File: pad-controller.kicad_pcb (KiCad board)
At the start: 2 copper layers, 32 parts, among them M1 Motor_Servo, M2 Motor_Servo, M3 Motor_Servo, M4 Motor_Servo, Q1 IRFP450PBF, SW1 SW_Push_Dual, U1 Xbee, U2 TPS56121, U3 LD1117S33TR_SOT223

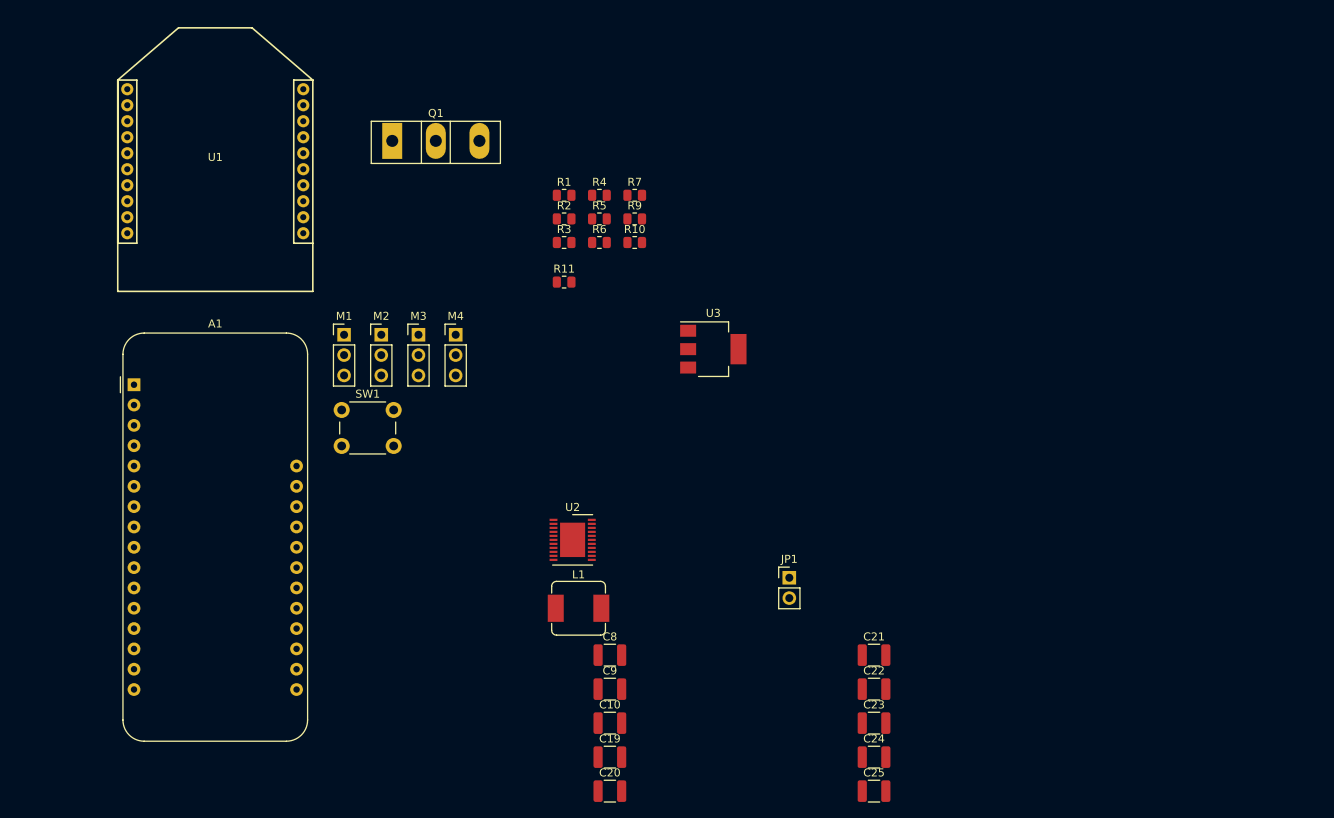
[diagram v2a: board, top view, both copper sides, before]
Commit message: Lay out the buck converter circuitry
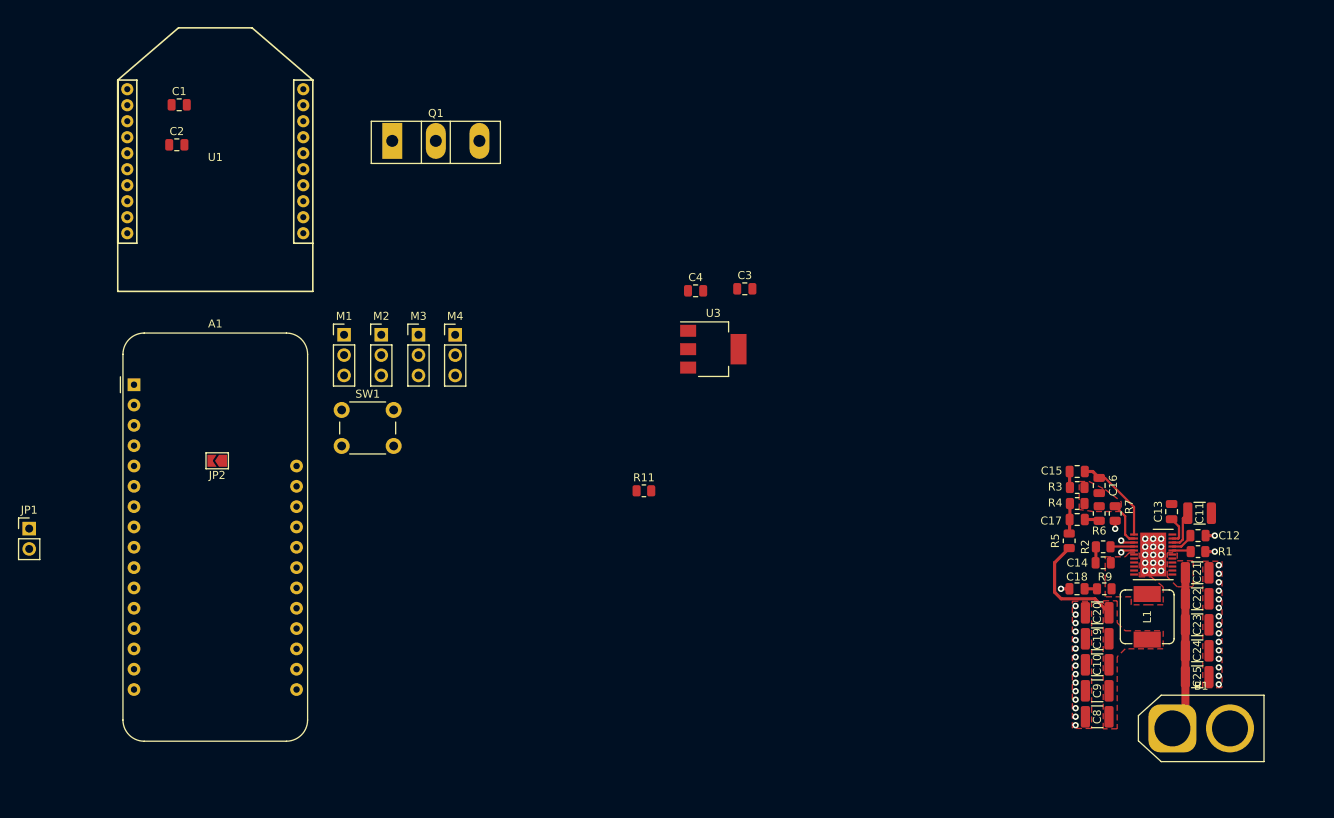
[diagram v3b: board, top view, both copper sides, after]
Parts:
- removed R10: 100 kΩ, Resistor_SMD:R_0805_2012Metric
- added B1: ~, Connector_AMASS:AMASS_XT60-M_1x02_P7.20mm_Vertical, F.Cu at (167.9, 121.7)
- added C1: 47 pF, Capacitor_SMD:C_0805_2012Metric, F.Cu at (43.8, 43.8)
- added C11: 1.0 uF, Capacitor_SMD:C_1210_3225Metric, F.Cu at (171.3, 94.8)
- added C12: 4.7 uF, Capacitor_SMD:C_0805_2012Metric, F.Cu at (171.1, 97.6)
- added C13: 33 nF, Capacitor_SMD:C_0805_2012Metric, F.Cu at (167.8, 94.6)
- added C14: 100 nF, Capacitor_SMD:C_0805_2012Metric, F.Cu at (159.2, 101.0)
- added C15: 390 pF, Capacitor_SMD:C_0805_2012Metric, F.Cu at (156.0, 89.6)
- added C16: 12 pF, Capacitor_SMD:C_0805_2012Metric, F.Cu at (158.8, 91.3)
- added C17: 820 pF, Capacitor_SMD:C_0805_2012Metric, F.Cu at (156.0, 95.6)
- added C18: 1000 pF, Capacitor_SMD:C_0805_2012Metric, F.Cu at (156.0, 104.2)
- added C2: 1 uF, Capacitor_SMD:C_0805_2012Metric, F.Cu at (43.5, 48.8)
- added C3: 10 uF, Capacitor_SMD:C_0805_2012Metric, F.Cu at (114.5, 66.8)
- added C4: 100 nF, Capacitor_SMD:C_0805_2012Metric, F.Cu at (108.3, 67.0)
- added JP2: ~, Jumper:SolderJumper-2_P1.3mm_Open_TrianglePad1.0x1.5mm, F.Cu at (48.5, 88.2)
- moved JP1 95.2 mm to (25.0, 96.7)
- moved R1 90.9 mm to (171.1, 99.6), turned to 180 degrees
- moved R2 78.9 mm to (159.2, 99.0), turned to 180 degrees
- moved R9 74.7 mm to (159.4, 104.2), turned to 180 degrees
- moved U2 72.6 mm to (165.5, 100.0)
- moved R7 72.0 mm to (160.8, 94.8), turned to -90 degrees
- moved R5 71.2 mm to (155.0, 98.2), turned to -90 degrees
- moved L1 71.1 mm to (164.8, 107.8), turned to -90 degrees
- moved R4 71.1 mm to (156.0, 93.6), turned to 180 degrees
- moved R3 71.1 mm to (156.0, 91.6)
- moved R6 71.1 mm to (158.8, 94.8), turned to -90 degrees
- moved C20 64.9 mm to (158.5, 107.2), turned to 180 degrees
- moved C19 62.7 mm to (158.5, 110.5), turned to 180 degrees
- moved C8 61.4 mm to (158.5, 120.2), turned to 180 degrees
- moved C10 61.3 mm to (158.5, 113.8), turned to 180 degrees
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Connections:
- net Net-(U2-ILIM) renamed /Power/ILIM
- A1 pad 17: unconnected-(A1-SDA-Pad17) -> Servo 3 PWM
- A1 pad 18: unconnected-(A1-SCL-Pad18) -> Servo 4 PWM
- A1 pad 19: TIM4 CH4 -> E-Match
- A1 pad 20: TIM4 CH3 -> Launch Inhibit
- A1 pad 21: TIM3 CH2 -> Servo 1 PWM
- A1 pad 22: TIM3 CH1 -> Servo 2 PWM
- A1 pad 9: E-Match -> unconnected-(A1-A4-Pad9)
- M1 pad 2: +3.3V -> +6V
- M1 pad 3: TIM3 CH1 -> Servo 1 PWM
- M2 pad 2: +3.3V -> +6V
- M2 pad 3: TIM3 CH2 -> Servo 2 PWM
- M3 pad 2: +3.3V -> +6V
- M3 pad 3: TIM4 CH3 -> Servo 3 PWM
- M4 pad 2: +3.3V -> +6V
- M4 pad 3: TIM4 CH4 -> Servo 4 PWM
- U2 pad 19: Power Good -> /Power/BP
- U2 pad 21: Net-(U2-EN/SS) -> /Power/EN/SS
- U2 pad 22: Net-(U2-PGOOD) -> unconnected-(U2-PGOOD-Pad22)
- U3 pad 1: unconnected-(U3-GND-Pad1) -> GND
- U3 pad 3: unconnected-(U3-VI-Pad3) -> +6V
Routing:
- net +BATT: track 0.00 -> 25.1 mm
- net +6V: track 0.00 -> 14.1 mm
- net /Power/Compensation: track 0.00 -> 11.4 mm
- net GND: track 0.00 -> 7.80 mm, vias 0 -> 51
- net /Power/Feedback: track 0.00 -> 5.37 mm
- net Net-(C17-Pad1): track 0.00 -> 3.79 mm
- net /Power/EN/SS: track 0.00 -> 3.58 mm
- net Net-(U2-BOOT): track 0.00 -> 2.96 mm
- net /Power/BP: track 0.00 -> 2.95 mm
- net /Power/ILIM: track 0.00 -> 2.35 mm
- net Net-(C14-Pad1): track 0.00 -> 2.02 mm
- net Net-(C15-Pad1): track 0.00 -> 2.02 mm
- net Net-(C17-Pad2): track 0.00 -> 1.87 mm
- net Net-(C18-Pad2): track 0.00 -> 1.55 mm
- added copper zone on F.Cu, net +6V
- added copper zone on F.Cu, net +BATT
- added copper zone on F.Cu, net /Power/Feedback
- added copper zone on F.Cu, net /Power/SW
- added copper zone on F.Cu, net GND

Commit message: Lay out the rest of the components
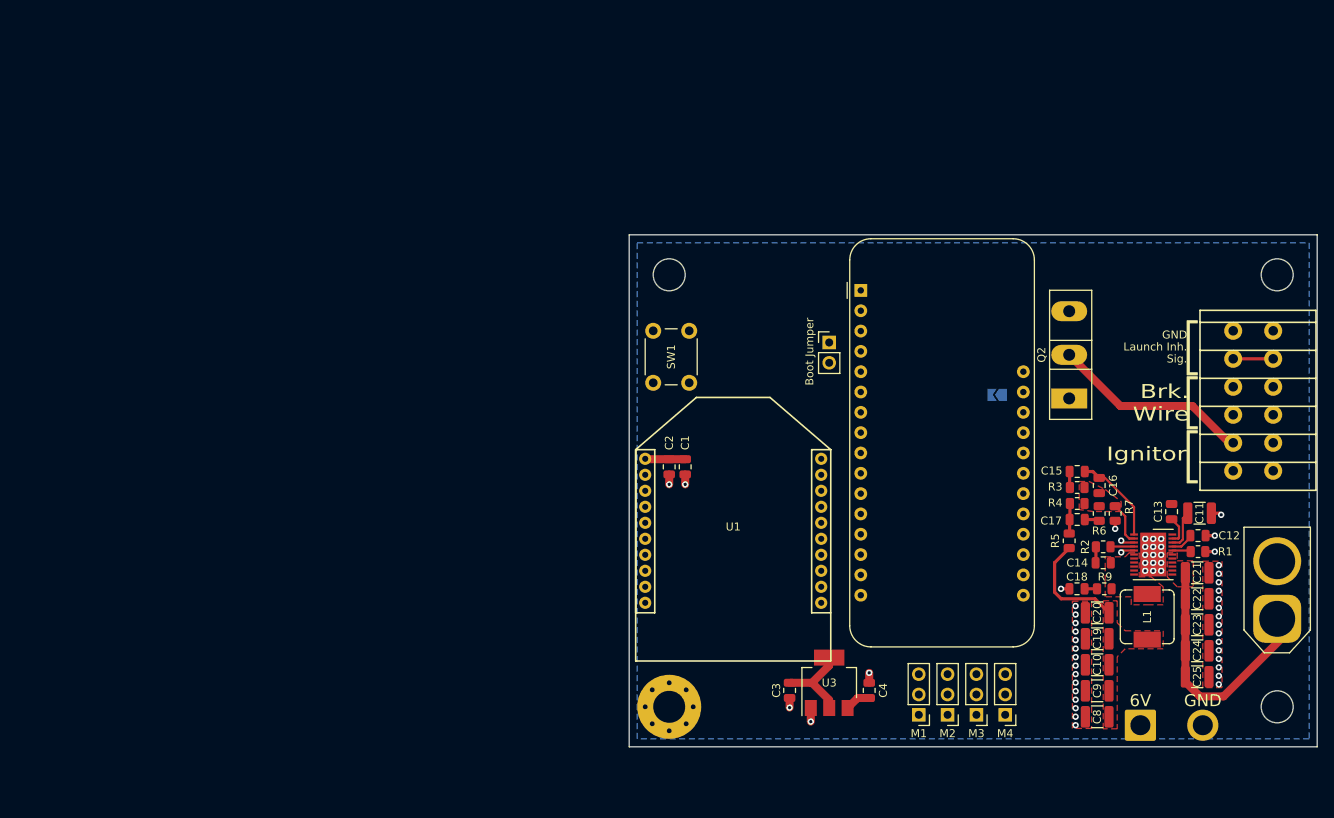
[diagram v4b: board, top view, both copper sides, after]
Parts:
- removed Q1: IRFP450PBF, Package_TO_SOT_THT:TO-247-3_Vertical
- removed R11: R, Resistor_SMD:R_0805_2012Metric
- added H1: MountingHole, MountingHole:MountingHole_4mm, F.Cu at (105.0, 65.0)
- added H2: MountingHole_Pad, MountingHole:MountingHole_4mm_Pad_Via, F.Cu at (105.0, 119.0)
- added H3: MountingHole, MountingHole:MountingHole_4mm, F.Cu at (181.0, 65.0)
- added H4: MountingHole, MountingHole:MountingHole_4mm, F.Cu at (181.0, 119.0)
- added J4: Conn_01x02, Connector_Wire:SolderWire-2sqmm_1x02_P7.8mm_D2mm_OD3.9mm, F.Cu at (163.9, 121.3)
- added J6: Conn_01x06, Marks_Footprints:WAGO_2601-1106_lever_terminal_block, F.Cu at (175.5, 72.0)
- added Q2: IRFP450PBF, Package_TO_SOT_THT:TO-247-3_Vertical, F.Cu at (155.0, 80.5)
- JP2: moved to B.Cu
- moved JP1 102.7 mm to (125.0, 73.5)
- moved JP2 97.8 mm to (146.0, 80.0)
- moved A1 91.6 mm to (128.9, 67.0)
- moved M1 86.1 mm to (136.2, 120.0), turned to 180 degrees
- moved M2 85.3 mm to (139.8, 120.0), turned to 180 degrees
- moved M3 84.4 mm to (143.4, 120.0), turned to 180 degrees
- moved M4 83.6 mm to (147.0, 120.0), turned to 180 degrees
- moved U1 79.5 mm to (113.0, 97.0)
- moved C1 77.8 mm to (107.0, 89.0), turned to -90 degrees
- moved C2 73.5 mm to (105.0, 89.0), turned to -90 degrees
- moved C4 54.5 mm to (130.0, 117.0), turned to 90 degrees
- moved C3 50.5 mm to (120.0, 117.0), turned to -90 degrees
- moved U3 44.1 mm to (125.0, 116.0), turned to 90 degrees
- moved SW1 39.1 mm to (103.0, 78.5), turned to 90 degrees
- moved B1 19.0 mm to (181.0, 108.0), turned to 90 degrees
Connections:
- A1 pad 10: Break Wire -> unconnected-(A1-A5-Pad10)
- A1 pad 17: Servo 3 PWM -> Servo 4 PWM
- A1 pad 18: Servo 4 PWM -> Servo 3 PWM
- A1 pad 19: E-Match -> unconnected-(A1-D0-Pad19)
- A1 pad 20: Launch Inhibit -> unconnected-(A1-D1-Pad20)
- A1 pad 21: Servo 1 PWM -> Servo 2 PWM
- A1 pad 22: Servo 2 PWM -> Servo 1 PWM
- A1 pad 23: Break Wire -> E-Match
- A1 pad 24: XBee RTS -> Break Wire
- A1 pad 25: XBee DTR -> Launch Inhibit
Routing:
- net Net-(J6-Pin_2): track 0.00 -> 24.6 mm
- net +3.3V: track 0.00 -> 15.9 mm
- net +BATT: track 25.1 -> 37.5 mm
- net GND: track 7.80 -> 15.8 mm, vias 51 -> 57
- net Launch Inhibit: track 0.00 -> 5.00 mm
- net +6V: track 14.1 -> 17.4 mm
- added copper zone on B.Cu, net GND
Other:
- board outline added: 86 x 64 mm
- board text added: "6V"
- board text added: "Brk. Wire"
- board text added: "GND"
- board text added: "Ignitor"
- board text added: "Launch Inh."
- board text added: "Sig."

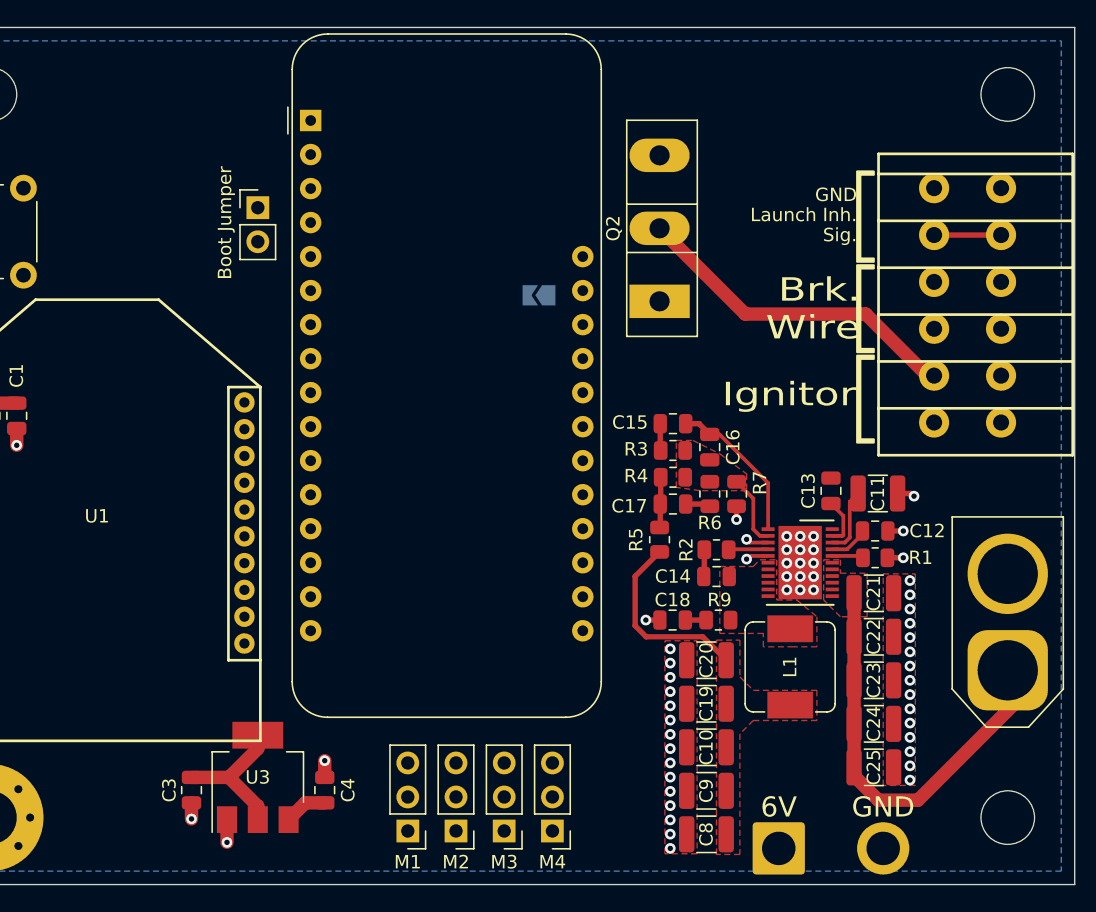
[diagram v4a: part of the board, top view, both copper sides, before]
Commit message: Replace ignitor mosfet with FQP30N06L
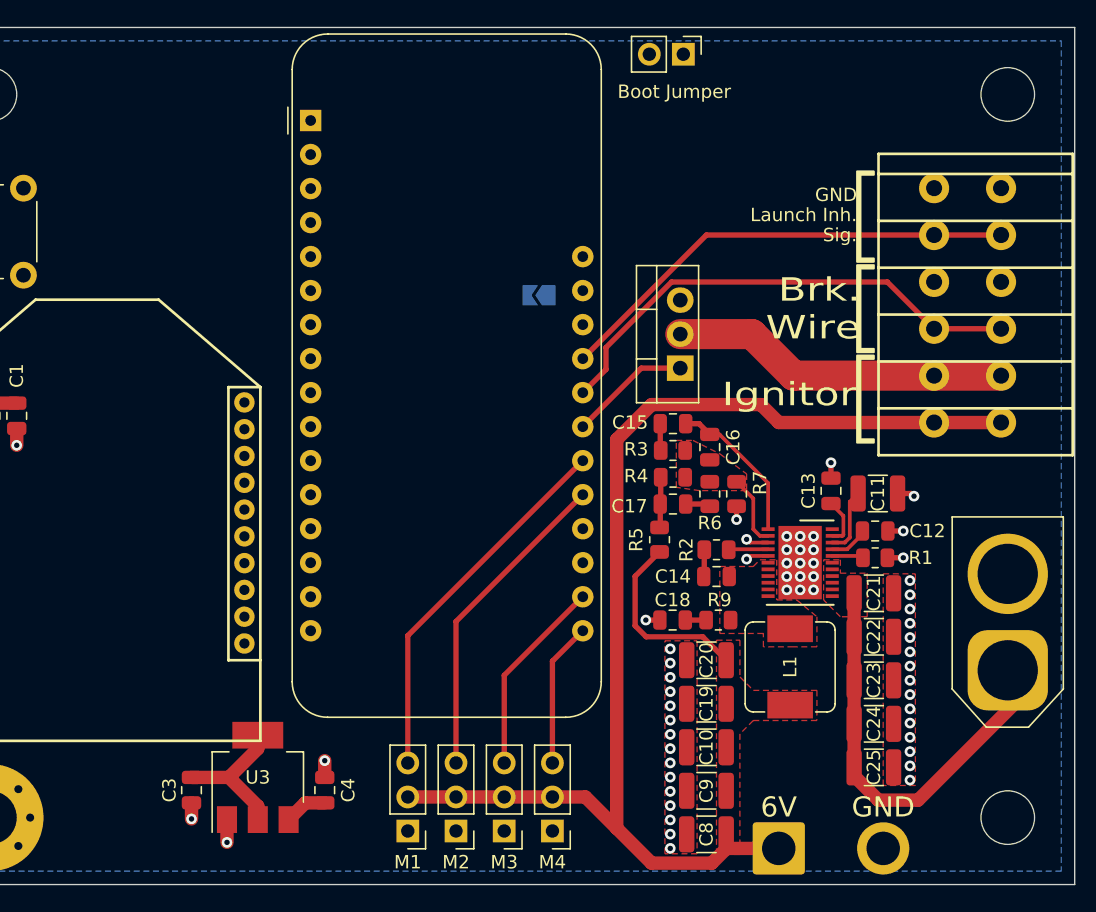
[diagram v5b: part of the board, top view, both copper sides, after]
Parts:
- Q2: value IRFP450PBF -> FQP30N06L; footprint Package_TO_SOT_THT:TO-247-3_Vertical -> Package_TO_SOT_THT:TO-220-3_Vertical
- moved JP1 33.8 mm to (156.8, 62.0), turned to -90 degrees
- moved Q2 5.22 mm to (156.5, 85.4)
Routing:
- net +6V: track 17.4 -> 108.0 mm
- net Break Wire: track 0.00 -> 37.1 mm
- net Launch Inhibit: track 5.00 -> 35.1 mm
- net Servo 1 PWM: track 0.00 -> 28.0 mm
- net Servo 2 PWM: track 0.00 -> 24.0 mm
- net Servo 3 PWM: track 0.00 -> 14.8 mm
- net Servo 4 PWM: track 0.00 -> 10.8 mm
- net E-Match: track 0.00 -> 9.09 mm
- net GND: track 15.8 -> 16.9 mm, vias 57 -> 58
- net Net-(J6-Pin_2): track 24.6 -> 25.2 mm

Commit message: Adjust layout
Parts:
- C11, C21: footprint Capacitor_SMD:C_1210_3225Metric -> Capacitor_SMD:C_0805_2012Metric
- C2: value 1 uF -> 1.0 uF
- U2: footprint Package_DFN_QFN:DFN-22-1EP_5x6mm_P0.5mm_EP3.14x4.3mm -> Marks_Footprints:DFN-22-1EP_5x6mm_P0.5mm_EP3.14x4.3mm
- moved JP1 54.2 mm to (124.8, 105.8), turned to 180 degrees
- moved SW1 23.2 mm to (110.6, 100.4), turned to 0 degrees
- moved U1 15.0 mm to (114.4, 82.1)
- moved C1 14.9 mm to (107.9, 74.1)
- moved C2 14.9 mm to (105.9, 74.1)
- moved Q2 3.10 mm to (154.4, 83.2), turned to 0 degrees
- moved B1 2.00 mm to (180.9, 110.0)
- moved U3 1.87 mm to (125.6, 117.8)
- moved C3 1.87 mm to (120.6, 118.7)
- moved C4 1.87 mm to (130.6, 118.7)
- moved C22 0.90 mm to (171.0, 104.6)
- moved C23 0.90 mm to (171.0, 107.8)
- moved C24 0.90 mm to (171.0, 111.1)
- moved C25 0.90 mm to (171.0, 114.3)
- moved C11 0.73 mm to (171.1, 95.5)
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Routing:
- net +3.3V: track 15.9 -> 97.1 mm
- net MCU TX: track 0.00 -> 36.1 mm
- net MCU RX: track 0.00 -> 35.8 mm
- net /XBee Reset: track 0.00 -> 28.8 mm
- net +6V: track 108.0 -> 118.6 mm
- net +BATT: track 37.5 -> 28.4 mm
- net Net-(A1-SPARE): track 0.00 -> 4.90 mm
- net Net-(A1-EN): track 0.00 -> 2.89 mm
- net Break Wire: track 37.1 -> 34.9 mm
- net GND: track 16.9 -> 16.7 mm, vias 58 -> 63
